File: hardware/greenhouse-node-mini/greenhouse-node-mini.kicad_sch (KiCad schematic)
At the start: 43 parts, among them J1 Molex_KK_396_1x2, J2 JST_XH_2.54mm_1x2, J4 Molex_KK_396_1x2, J5 JST_XH_2.54mm_1x4, J6 PinHeader_1x04_P2.54mm, J7 PinHeader_1x04_P2.54mm, Q1 A42, SW1 SW_Push, U1 ATtiny84A-P, U2 L7805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

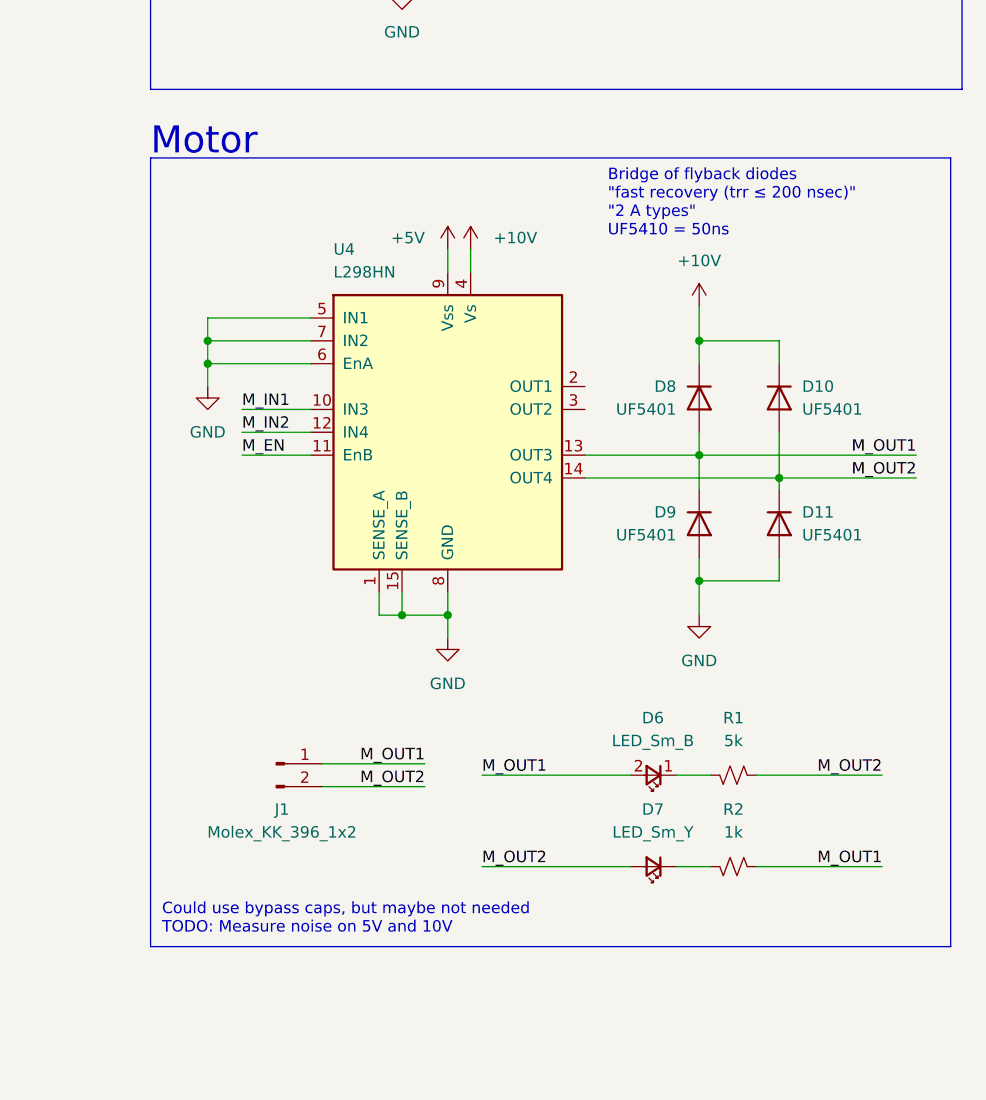
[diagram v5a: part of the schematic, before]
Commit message: Change notes on node schematic
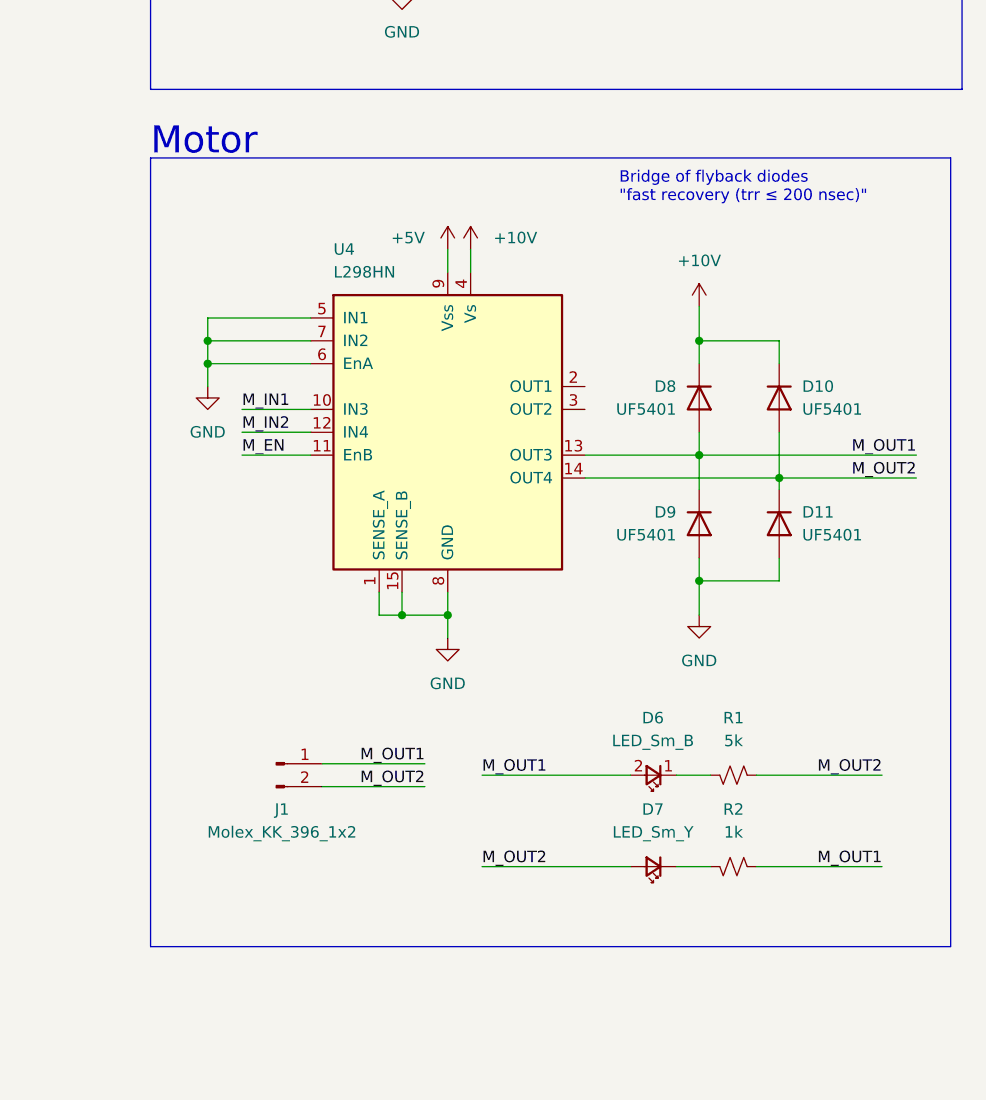
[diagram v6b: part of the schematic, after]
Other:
- note added: "Bridge of flyback diodes "fast recovery (trr ≤ 200 nsec)""
- note removed: "Bridge of flyback diodes "fast recovery (trr ≤ 200 nsec)" "2 A types" UF5410 = 50ns"
- note removed: "Could use bypass caps, but maybe not needed TODO: Measure noise on 5V and 10V"
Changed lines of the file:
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@@
     (effects (font (size 3 3)) (justify left bottom))
-  )
-  (text "Could use bypass caps, but maybe not needed\nTODO: Measure noise on 5V and 10V"
-    (at 171.45 161.29 0)
-    (effects (font (size 1.27 1.27)) (justify left bottom))
   )
   (text "Power" (at 26.67 19.05 0)
@@
     (effects (font (size 1.27 1.27)) (justify left bottom))
   )
-  (text "Bridge of flyback diodes\n\"fast recovery (trr ≤ 200 nsec)\" \n\"2 A types\"\nUF5410 = 50ns"
-    (at 220.98 83.82 0)
+  (text "Bridge of flyback diodes\n\"fast recovery (trr ≤ 200 nsec)\""
+    (at 222.25 80.01 0)
     (effects (font (size 1.27 1.27)) (justify left bottom))
   )

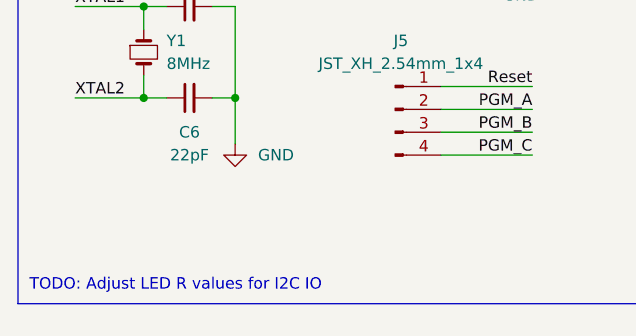
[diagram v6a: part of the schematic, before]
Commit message: Reorganize schematics
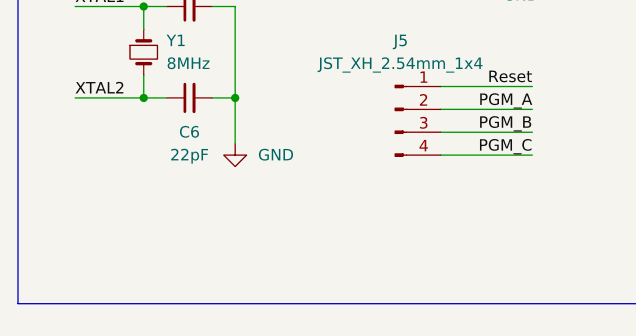
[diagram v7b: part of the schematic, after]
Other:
- note removed: "TODO: Adjust LED R values for I2C IO"
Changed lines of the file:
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@@
     (effects (font (size 3 3)) (justify left bottom))
-  )
-  (text "TODO: Adjust LED R values for I2C IO" (at 27.94 194.31 0)
-    (effects (font (size 1.27 1.27)) (justify left bottom))
   )
   (text "Bridge of flyback diodes\n\"fast recovery (trr ≤ 200 nsec)\""

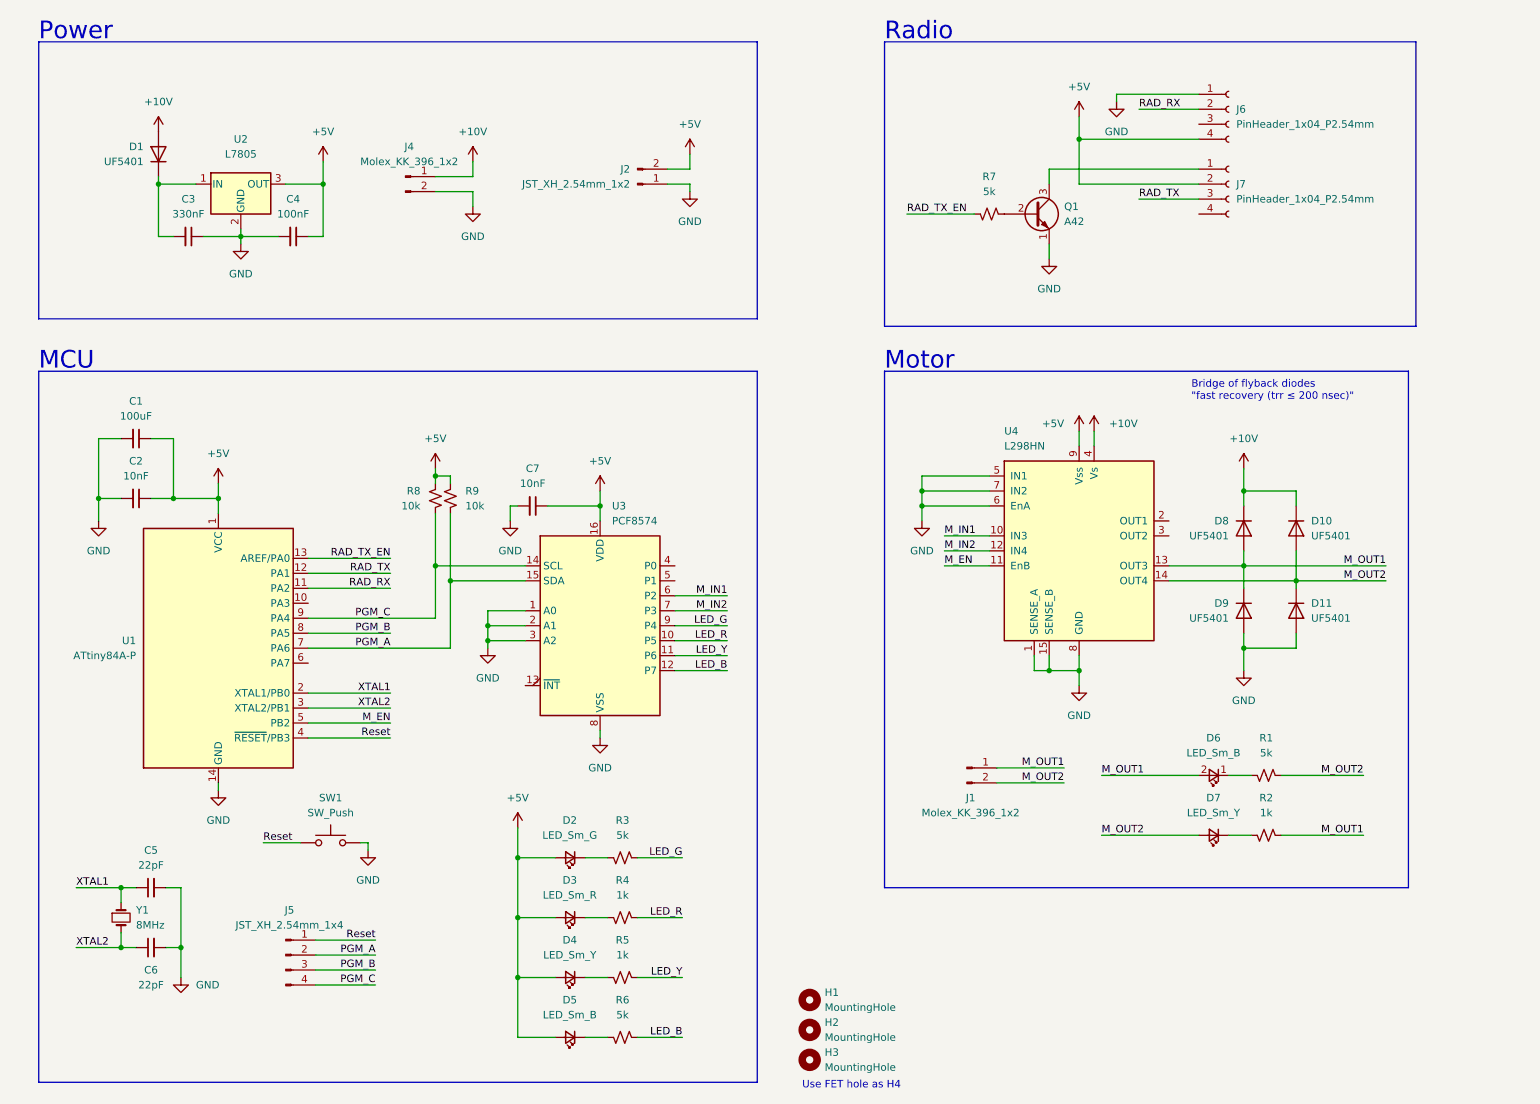
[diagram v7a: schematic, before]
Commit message: Replace RX/TX modules with HC-12
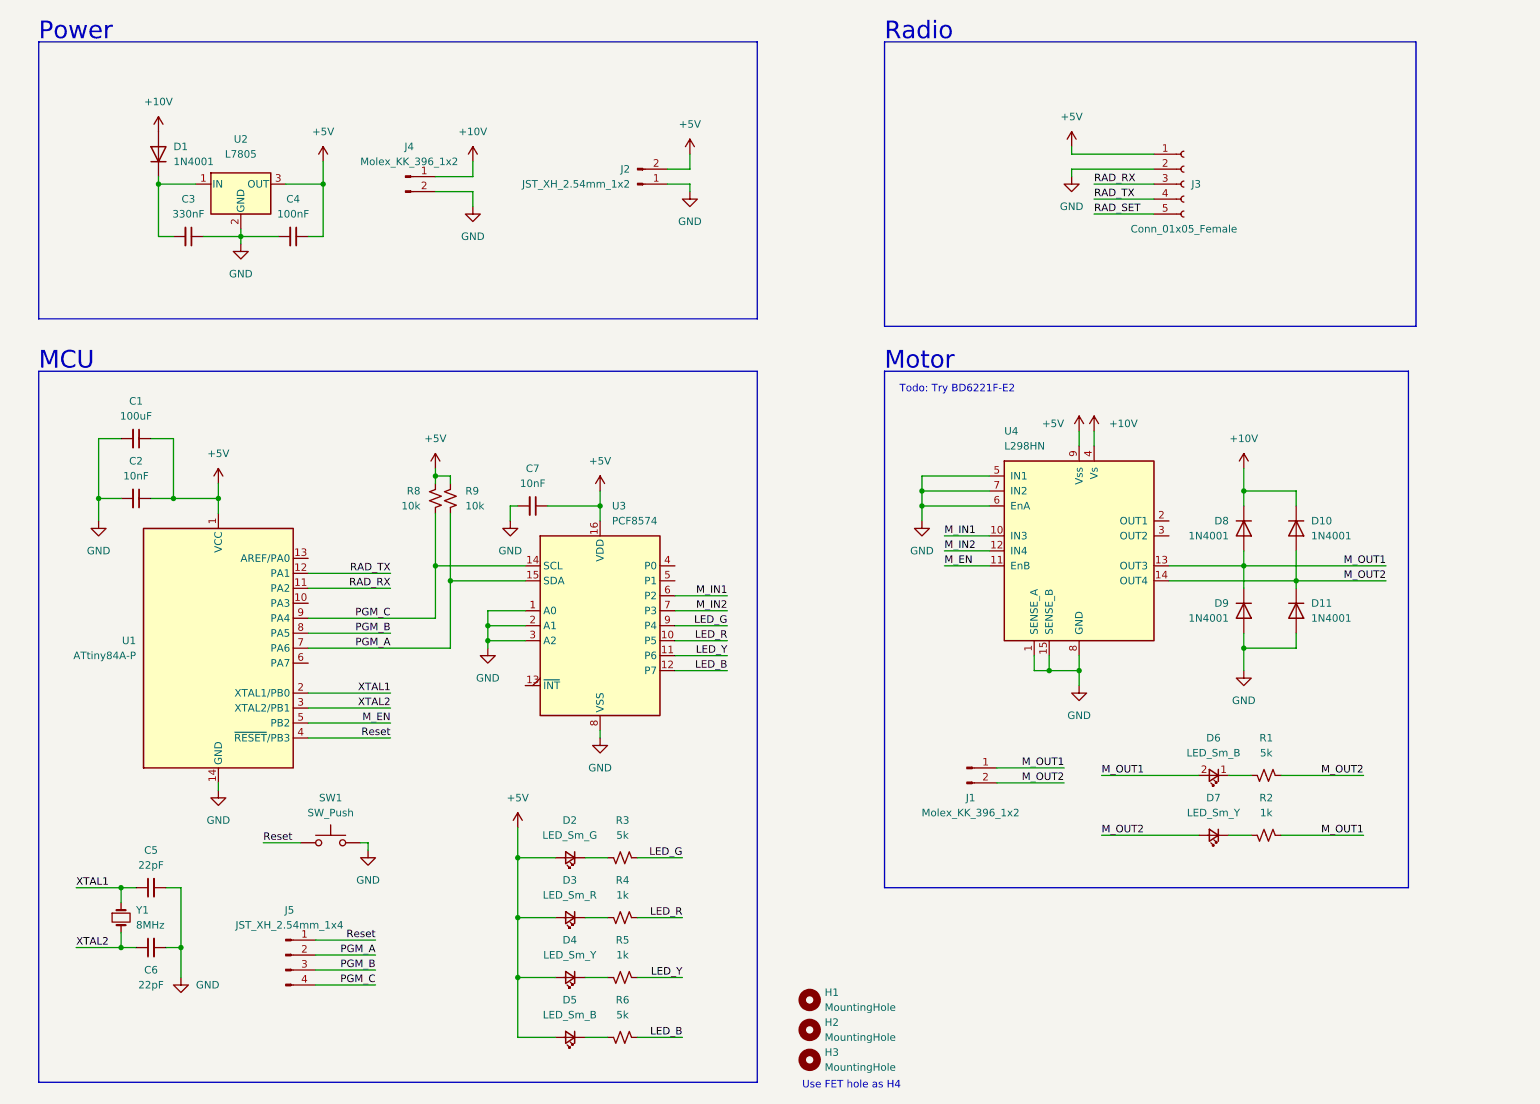
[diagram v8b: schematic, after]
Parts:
- removed J6, J7: PinHeader_1x04_P2.54mm, Connector_PinSocket_2.54mm:PinSocket_1x04_P2.54mm_Vertical, symbol Connector:Conn_01x04_Female
- removed Q1: A42, Package_TO_SOT_THT:TO-92_Inline, symbol Device:Q_NPN_EBC
- removed R7: 5k, Resistor_THT:R_Axial_DIN0204_L3.6mm_D1.6mm_P7.62mm_Horizontal, symbol Device:R_Small_US
- added J3: Conn_01x05_Female, Connector_PinSocket_2.54mm:PinSocket_1x05_P2.54mm_Vertical, symbol Connector:Conn_01x05_Female
- D1, D10, D11, D8, D9: value UF5401 -> 1N4001; footprint Diode_THT:D_DO-201AD_P15.24mm_Horizontal -> Diode_THT:D_DO-41_SOD81_P7.62mm_Horizontal; symbol Diode:UF5401 -> Diode:1N4001
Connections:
- net +5V: now also J3.1 (Pin_1)
- net GND: now also J3.2 (Pin_2)
- net RAD_RX: now also J3.3 (Pin_3)
- net RAD_TX: now also J3.4 (Pin_4)
- net RAD_TX_EN: no longer names the net of U1.13 (AREF/PA0)
- new net RAD_SET: J3.5 (Pin_5)
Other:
- note added: "Todo: Try BD6221F-E2"
- note removed: "Bridge of flyback diodes "fast recovery (trr ≤ 200 nsec)""
